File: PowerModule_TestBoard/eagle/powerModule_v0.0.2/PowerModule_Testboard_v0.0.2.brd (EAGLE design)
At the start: 80 x 57.1 mm, 43 parts, among them J1 1X2-3.5MM, J12 TP_OPEN, J4 1X2-3.5MM, J5 1X2-3.5MM

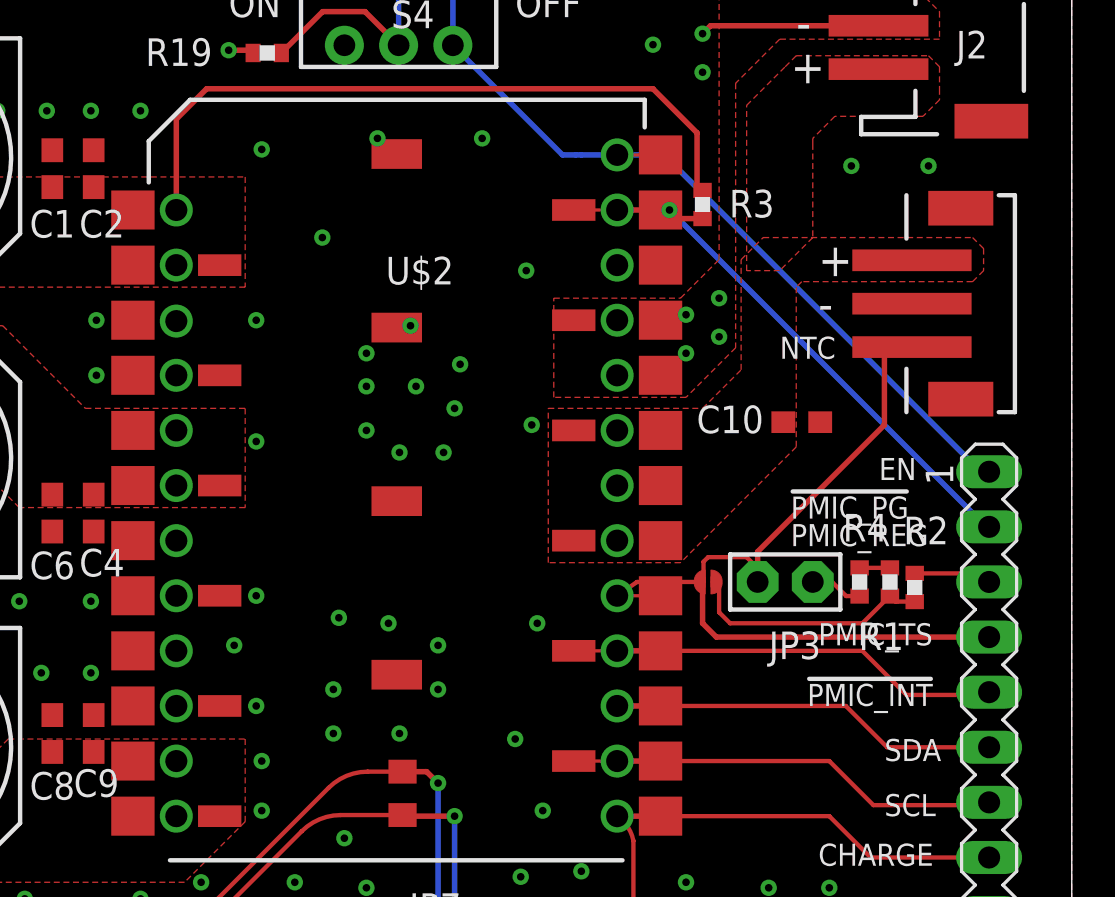
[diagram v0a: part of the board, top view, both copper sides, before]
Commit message: update the power module v0.0.2
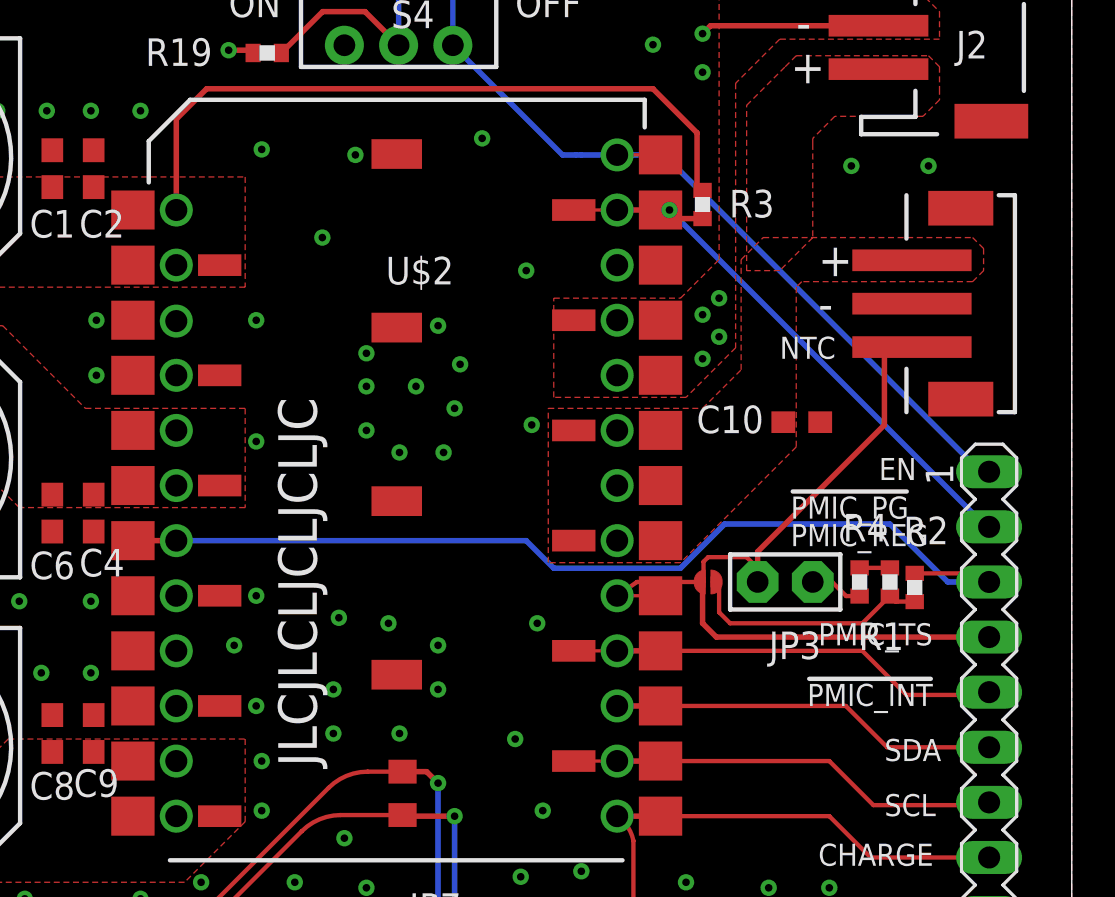
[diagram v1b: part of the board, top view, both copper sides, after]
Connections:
- removed net PMIC_REG: R1.2, SV1.3
- net PMIC_RGEN: now also R1.2, SV1.3
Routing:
- net PMIC_RGEN: track 0.00 -> 46.9 mm
- net PMIC_REG: track 3.59 -> 0.00 mm
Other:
- board text added: "JLCJLCLJCLJCLJC"
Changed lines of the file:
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@@
 <wire x1="0" y1="1.27" x2="1.27" y2="0" width="0" layer="20"/>
 <text x="29.21" y="2.54" size="1.778" layer="21" ratio="20">Power module EVB v0.0.2</text>
+<text x="45.212" y="18.796" size="1.778" layer="21" rot="R90">JLCJLCLJCLJCLJC</text>
 </plain>
 <attributes>
@@
 <via x="51.562" y="35.306" extent="1-16" drill="0.35"/>
 <via x="51.816" y="37.338" extent="1-16" drill="0.35"/>
-<via x="49.53" y="39.116" extent="1-16" drill="0.35"/>
+<via x="50.8" y="39.116" extent="1-16" drill="0.35"/>
 <via x="49.784" y="36.322" extent="1-16" drill="0.35"/>
 <via x="50.8" y="22.352" extent="1-16" drill="0.35"/>
@@
 <via x="54.864" y="41.656" extent="1-16" drill="0.35"/>
 <via x="42.672" y="47.244" extent="1-16" drill="0.35"/>
-<via x="48.006" y="47.752" extent="1-16" drill="0.35"/>
+<via x="46.99" y="46.99" extent="1-16" drill="0.35"/>
 <via x="52.832" y="47.752" extent="1-16" drill="0.35"/>
 <via x="3.556" y="25.908" extent="1-16" drill="0.35"/>
@@
 <via x="66.04" y="5.842" extent="1-16" drill="0.35"/>
 <via x="70.612" y="5.842" extent="1-16" drill="0.35"/>
-<via x="62.23" y="39.624" extent="1-16" drill="0.35"/>
-<via x="62.23" y="37.846" extent="1-16" drill="0.35"/>
+<via x="62.992" y="39.624" extent="1-16" drill="0.35"/>
+<via x="62.992" y="37.592" extent="1-16" drill="0.35"/>
 <via x="63.754" y="40.386" extent="1-16" drill="0.35"/>
 <via x="63.754" y="38.608" extent="1-16" drill="0.35"/>
@@
 <wire x1="61.055" y1="16.51" x2="59.182" y2="16.51" width="0.254" layer="1"/>
 </signal>
-<signal name="PMIC_REG">
+<signal name="PMIC_RGEN">
+<contactref element="U$2" pad="7"/>
+<contactref element="U$2" pad="7@1"/>
+<wire x1="38.735" y1="29.21" x2="37.338" y2="29.21" width="0.1524" layer="1"/>
 <contactref element="SV1" pad="3"/>
 <contactref element="R1" pad="2"/>
 <wire x1="72.771" y1="27.701" x2="75.804" y2="27.701" width="0.2" layer="1"/>
 <wire x1="75.804" y1="27.701" x2="76.2" y2="27.305" width="0.2" layer="1"/>
-</signal>
-<signal name="PMIC_RGEN">
-<contactref element="U$2" pad="7"/>
-<contactref element="U$2" pad="7@1"/>
-<wire x1="36.735" y1="29.21" x2="38.735" y2="29.21" width="0" layer="19" extent="1-1"/>
+<wire x1="38.735" y1="29.21" x2="54.864" y2="29.21" width="0.254" layer="16"/>
+<wire x1="54.864" y1="29.21" x2="56.134" y2="27.94" width="0.254" layer="16"/>
+<wire x1="56.134" y1="27.94" x2="61.976" y2="27.94" width="0.254" layer="16"/>
+<wire x1="74.295" y1="27.305" x2="76.2" y2="27.305" width="0.254" layer="16"/>
+<wire x1="61.976" y1="27.94" x2="64.008" y2="29.972" width="0.254" layer="16"/>
+<wire x1="64.008" y1="29.972" x2="71.628" y2="29.972" width="0.254" layer="16"/>
+<wire x1="71.628" y1="29.972" x2="74.295" y2="27.305" width="0.254" layer="16"/>
+<wire x1="36.735" y1="29.21" x2="38.735" y2="29.21" width="0.254" layer="1"/>
 </signal>
 <signal name="+5V">
